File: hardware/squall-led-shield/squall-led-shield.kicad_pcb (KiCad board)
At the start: 2 copper layers, 25.4 x 21 mm, 19 parts, among them J1 SQUALL_HEADER, J2 TC2030, J3 TACK_PAD, J4 TACK_PAD, Q1 Q_2NMOS

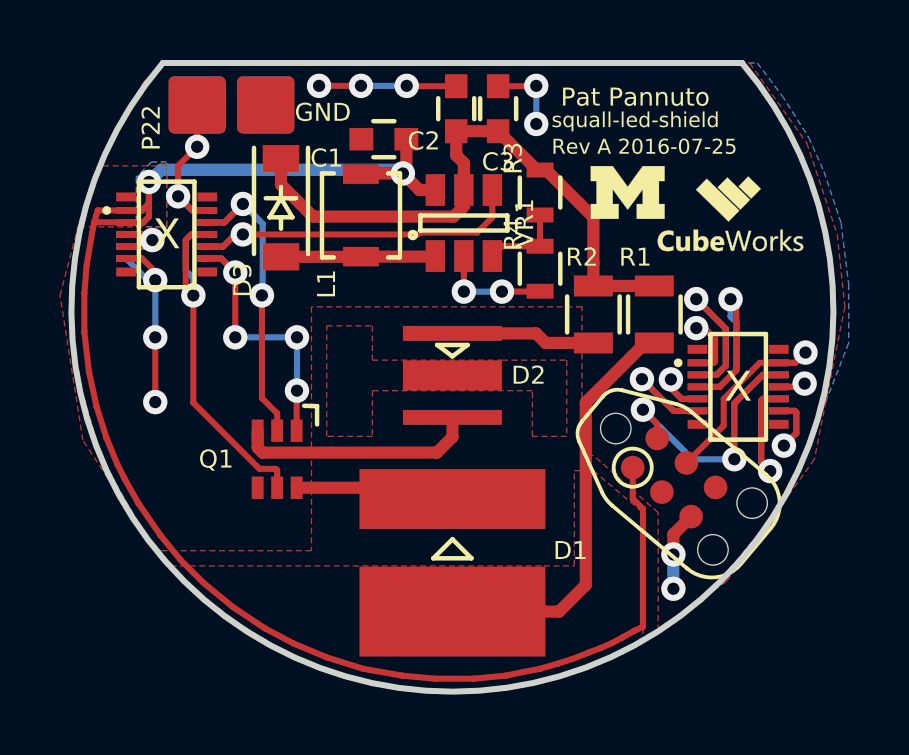
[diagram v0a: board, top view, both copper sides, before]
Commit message: Clean up fill around pad a bit
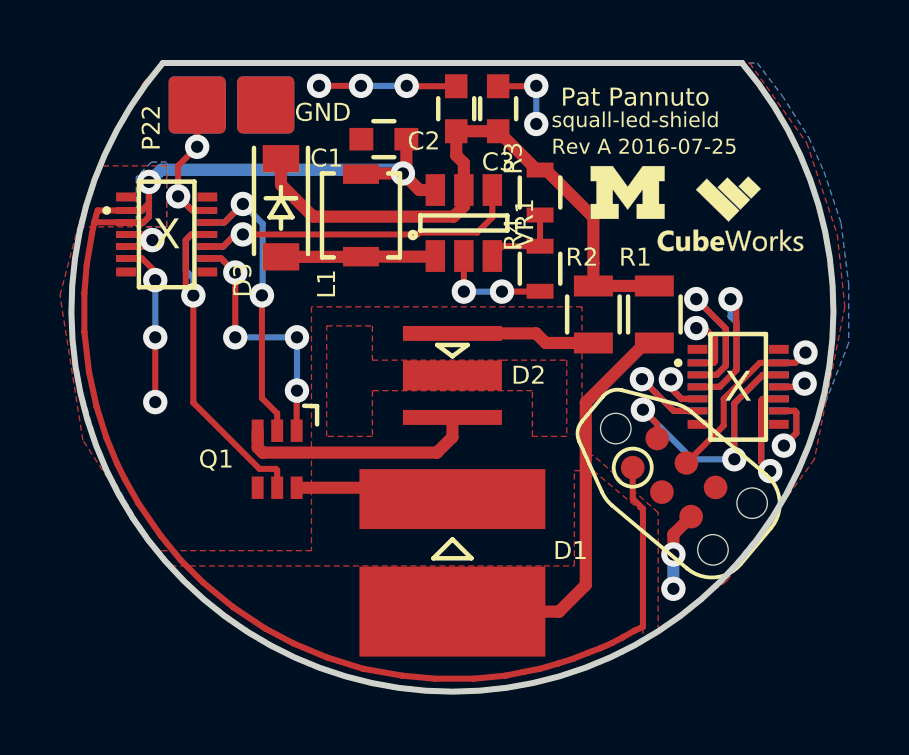
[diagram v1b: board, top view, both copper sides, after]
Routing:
- net GND: track 29.9 -> 28.6 mm
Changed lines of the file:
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@@
     (thickness 1.6)
     (drawings 9)
-    (tracks 303)
+    (tracks 301)
     (zones 0)
     (modules 19)
@@
   (segment (start 147.20824 104.27716) (end 147.2184 104.267) (width 0.2032) (layer F.Cu) (net 1))
   (via (at 147.2184 104.267) (size 0.8128) (drill 0.4064) (layers F.Cu B.Cu) (net 1))
-  (segment (start 142.494 100.584) (end 142.244 100.584) (width 0.2032) (layer B.Cu) (net 1))
-  (segment (start 142.244 100.584) (end 141.52 99.86) (width 0.2032) (layer B.Cu) (net 1))
   (segment (start 142.494 102.489) (end 142.494 104.648) (width 0.2032) (layer F.Cu) (net 1))
   (via (at 142.494 104.648) (size 0.8128) (drill 0.4064) (layers F.Cu B.Cu) (net 1))
@@
     (connect_pads (clearance 0.2032))
     (min_thickness 0.2032)
-    (fill yes (arc_segments 32) (thermal_gap 0.254) (thermal_bridge_width 0.508))
+    (fill yes (arc_segments 32) (thermal_gap 0.254) (thermal_bridge_width 0.254))
     (polygon
       (pts

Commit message: Clean up silkscreen
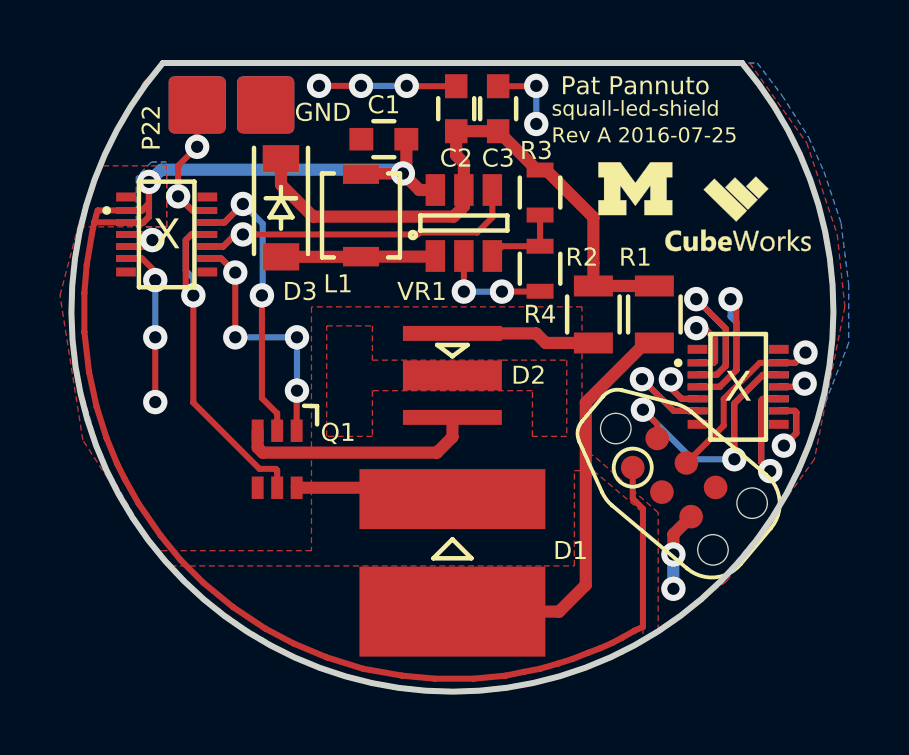
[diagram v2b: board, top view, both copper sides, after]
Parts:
- moved _2 0.28 mm to (158.5, 97.5)
- moved _1 0.25 mm to (161.9, 98.4)
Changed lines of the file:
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@@
   (general
     (links 58)
-    (no_connects 0)
-    (area 137.2318 89.9713 282.218715 163.828)
+    (no_connects 10)
+    (area 139.599364 93.244999 165.200636 114.400636)
     (thickness 1.6)
     (drawings 9)
@@
     (tags "capacitor 0603")
     (attr smd)
-    (fp_text reference C1 (at 1.905 -0.635) (layer F.SilkS)
+    (fp_text reference C1 (at 0 1.143) (layer F.SilkS)
       (effects (font (size 0.6 0.6) (thickness 0.1)))
     )
@@
     (tags SC-70-6,)
     (attr smd)
-    (fp_text reference Q1 (at 2.032 0 180) (layer F.SilkS)
+    (fp_text reference Q1 (at -2.032 0.889 180) (layer F.SilkS)
       (effects (font (size 0.6 0.6) (thickness 0.1)))
     )
@@
     (tags "capacitor 0603")
     (attr smd)
-    (fp_text reference C2 (at -1.0795 -1.0795 -180) (layer F.SilkS)
+    (fp_text reference C2 (at -1.651 0 -180) (layer F.SilkS)
       (effects (font (size 0.6 0.6) (thickness 0.1)))
     )
@@
   (module Squall:INDUCTOR_VLF (layer F.Cu)
     (at 149.352 98.425 270)
-    (fp_text reference L1 (at 2.286 1.143 90) (layer F.SilkS)
+    (fp_text reference L1 (at 2.286 0.762 180) (layer F.SilkS)
       (effects (font (size 0.6 0.6) (thickness 0.1)))
     )
@@
     (tags SOT-23-6)
     (attr smd)
-    (fp_text reference VR1 (at 0 2.032 90) (layer F.SilkS)
+    (fp_text reference VR1 (at -2.286 -1.397 180) (layer F.SilkS)
       (effects (font (size 0.6 0.6) (thickness 0.1)))
     )
@@
   )
   (module Squall:CubeWorks_Logo-5mm (layer F.Cu)
-    (at 161.671 98.425)
+    (at 161.925 98.425)
     (fp_text reference _1 (at 0 0) (layer F.SilkS) hide
       (effects (font (thickness 0.3)))
@@
     (tags "capacitor 0603")
     (attr smd)
-    (fp_text reference C3 (at -1.778 0 -180) (layer F.SilkS)
+    (fp_text reference C3 (at -1.651 0 -180) (layer F.SilkS)
       (effects (font (size 0.6 0.6) (thickness 0.1)))
     )
@@
     (tags SOD-123)
     (attr smd)
-    (fp_text reference D3 (at 2.413 1.27 90) (layer F.SilkS)
+    (fp_text reference D3 (at 2.794 -0.635 180) (layer F.SilkS)
       (effects (font (size 0.6 0.6) (thickness 0.1)))
     )
@@
     (tags "resistor 0603")
     (attr smd)
-    (fp_text reference R3 (at -1.143 0.889 90) (layer F.SilkS)
+    (fp_text reference R3 (at -1.397 0.127 180) (layer F.SilkS)
       (effects (font (size 0.6 0.6) (thickness 0.1)))
     )
@@
     (tags "resistor 0603")
     (attr smd)
-    (fp_text reference R4 (at -1.143 0.889 90) (layer F.SilkS)
+    (fp_text reference R4 (at 1.524 0 180) (layer F.SilkS)
       (effects (font (size 0.6 0.6) (thickness 0.1)))
     )
@@
   )
   (module Logos:BLOCK_M_SOLID_100MIL (layer F.Cu)
-    (at 158.242 97.663)
+    (at 158.496 97.536)
     (fp_text reference _2 (at 0 0) (layer F.SilkS) hide
       (effects (font (thickness 0.3)))
@@
   )
   (gr_arc (start 152.4 101.6) (end 158.7246 112.141) (angle 136.8114615) (layer Dwgs.User) (width 0.2))
-  (gr_text "Rev A 2016-07-25" (at 155.702 96.139) (layer F.SilkS)
+  (gr_text "Rev A 2016-07-25" (at 155.702 95.758) (layer F.SilkS)
     (effects (font (size 0.5 0.5) (thickness 0.05)) (justify left))
   )
-  (gr_text squall-led-shield (at 155.702 95.25) (layer F.SilkS)
+  (gr_text squall-led-shield (at 155.702 94.869) (layer F.SilkS)
     (effects (font (size 0.5 0.5) (thickness 0.05)) (justify left))
   )
-  (gr_text "Pat Pannuto" (at 158.496 94.488) (layer F.SilkS)
+  (gr_text "Pat Pannuto" (at 158.496 94.107) (layer F.SilkS)
     (effects (font (size 0.6 0.6) (thickness 0.05)))
   )

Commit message: Fixup outline to touch
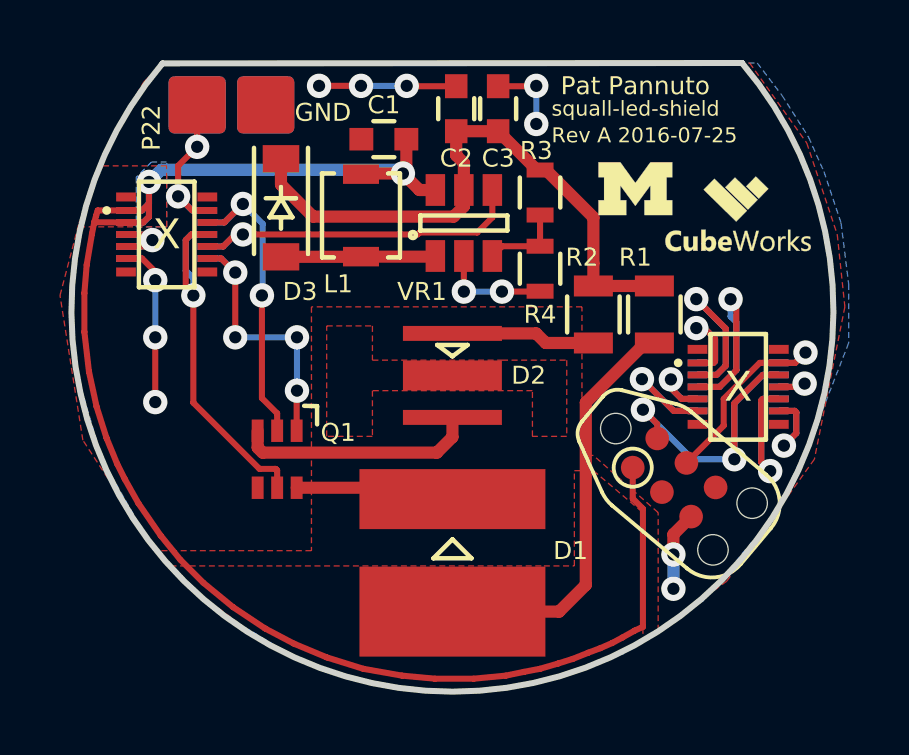
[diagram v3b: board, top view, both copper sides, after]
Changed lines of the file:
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@@
     (effects (font (size 0.6 0.6) (thickness 0.05)))
   )
-  (gr_line (start 142.748 93.345) (end 162.052 93.345) (layer Edge.Cuts) (width 0.2))
+  (gr_line (start 142.736727 93.358199) (end 162.052 93.345) (layer Edge.Cuts) (width 0.2))
   (gr_text "Squall shield format is 261 degrees of a circle from (380,325mil) to (-380, 325mil)" (at 232.283 162.433) (layer F.Fab)
     (effects (font (size 1.5 1.5) (thickness 0.3)))

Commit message: Fix date
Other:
- board text added: "Rev A 2016-07-26"
- board text removed: "Rev A 2016-07-25"
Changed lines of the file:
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@@
   (general
     (links 58)
-    (no_connects 10)
-    (area 139.599364 93.244999 165.200636 114.400636)
+    (no_connects 1)
+    (area 137.2318 89.9713 282.218715 163.828)
     (thickness 1.6)
     (drawings 9)
@@
   )
   (gr_arc (start 152.4 101.6) (end 158.7246 112.141) (angle 136.8114615) (layer Dwgs.User) (width 0.2))
-  (gr_text "Rev A 2016-07-25" (at 155.702 95.758) (layer F.SilkS)
+  (gr_text "Rev A 2016-07-26" (at 155.702 95.758) (layer F.SilkS)
     (effects (font (size 0.5 0.5) (thickness 0.05)) (justify left))
   )

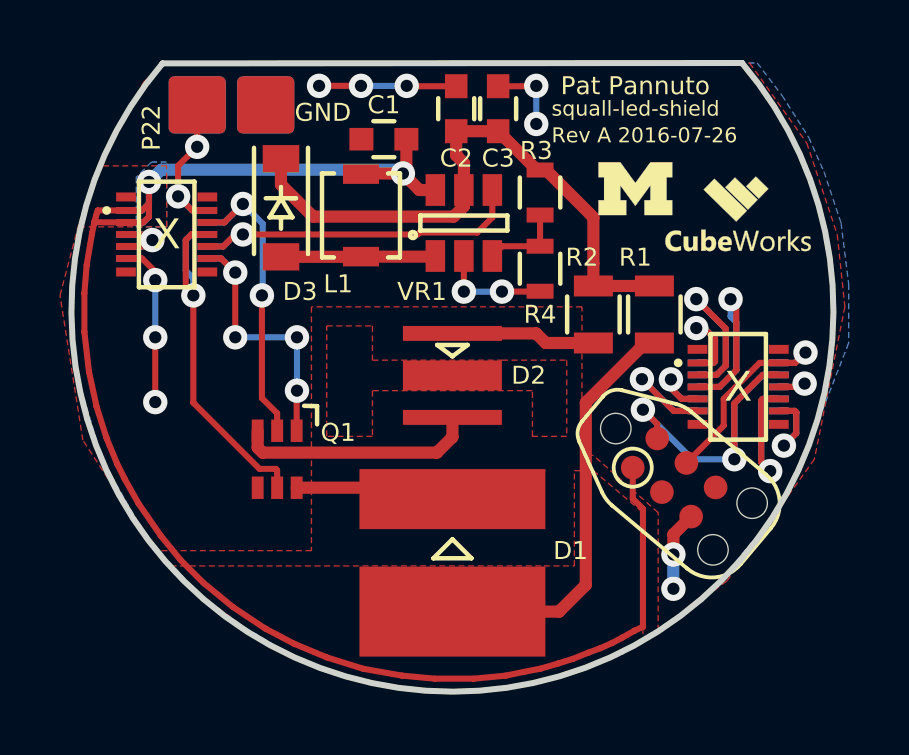
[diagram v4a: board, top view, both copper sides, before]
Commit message: Appease fill around gnd pad
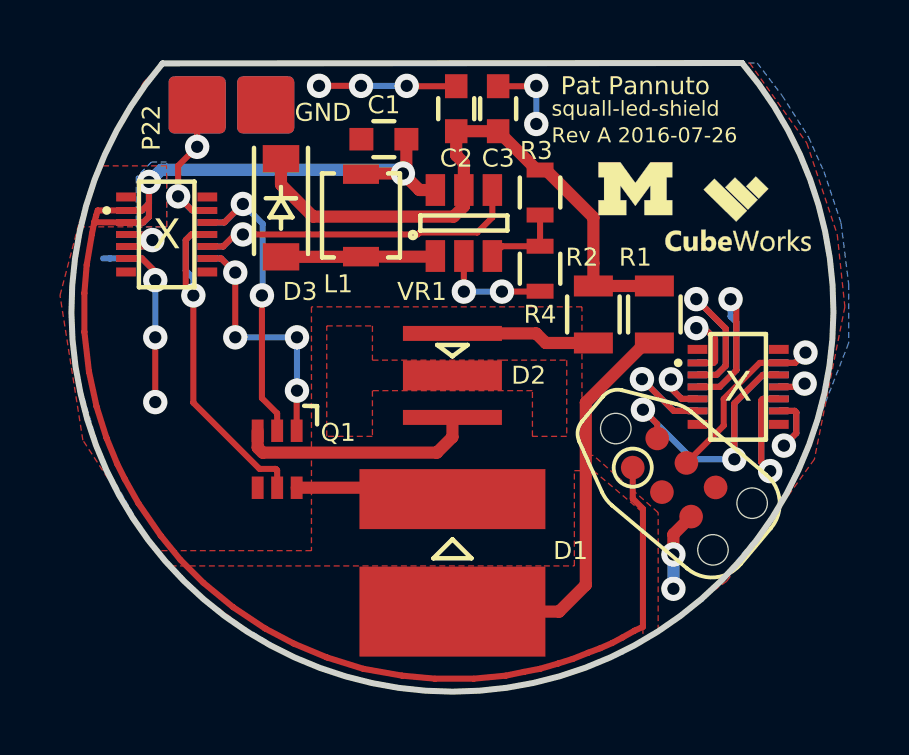
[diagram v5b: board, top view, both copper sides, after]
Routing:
- net GND: track 28.6 -> 30.8 mm
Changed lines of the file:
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@@
   (general
     (links 58)
-    (no_connects 1)
+    (no_connects 0)
     (area 137.2318 89.9713 282.218715 163.828)
     (thickness 1.6)
     (drawings 9)
-    (tracks 301)
+    (tracks 307)
     (zones 0)
     (modules 19)
@@
   )
   (gr_arc (start 152.4 101.6) (end 162.052 93.345) (angle 261) (layer Edge.Cuts) (width 0.2))
+  (segment (start 142.494 100.584) (end 142.494 100.3046) (width 0.2032) (layer B.Cu) (net 1))
+  (segment (start 142.494 100.3046) (end 142.0494 99.86) (width 0.2032) (layer B.Cu) (net 1))
+  (segment (start 142.0494 99.86) (end 141.52 99.86) (width 0.2032) (layer B.Cu) (net 1))
+  (segment (start 140.9867 99.8601) (end 140.7541 99.8601) (width 0.2032) (layer B.Cu) (net 1))
+  (segment (start 141.52 99.86) (end 140.9868 99.86) (width 0.2032) (layer B.Cu) (net 1))
+  (segment (start 140.9868 99.86) (end 140.9867 99.8601) (width 0.2032) (layer B.Cu) (net 1))
   (segment (start 144.23 99.86) (end 144.691 99.86) (width 0.2032) (layer F.Cu) (net 1))
   (segment (start 144.691 99.86) (end 145.161 100.33) (width 0.2032) (layer F.Cu) (net 1))
